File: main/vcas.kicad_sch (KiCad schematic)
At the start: 52 parts, among them U28 TL072CP, U29 TL072CP, U30 NSL-32SR3, U31 NSL-32SR3, U32 TL072CP, U33 TL072CP, U34 NSL-32SR3, U35 NSL-32SR3

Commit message: Switch to Thonk jacks.
Reduces use of extended parts.
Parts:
- C76, C77, C78, C79: LCSC Part # C277470 -> C45783
- R113, R116, R123, R126: LCSC Part # C136589 -> C4184
- U28, U29, U32, U33: LCSC Part # C67473 -> C6961
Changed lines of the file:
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@@
       (effects (font (size 1.27 1.27)) hide)
     )
-    (property "LCSC Part #" "C136589" (id 5) (at 149.86 120.015 0)
+    (property "LCSC Part #" "C4184" (id 5) (at 149.86 120.015 0)
       (effects (font (size 1.27 1.27)) hide)
     )
@@
       (effects (font (size 1.27 1.27)) hide)
     )
-    (property "LCSC Part #" "C67473" (id 6) (at 54.61 121.92 0)
+    (property "LCSC Part #" "C6961" (id 6) (at 54.61 121.92 0)
       (effects (font (size 1.27 1.27)) hide)
     )
@@
       (effects (font (size 1.27 1.27)) hide)
     )
-    (property "LCSC Part #" "C136589" (id 5) (at 148.59 52.07 0)
+    (property "LCSC Part #" "C4184" (id 5) (at 148.59 52.07 0)
       (effects (font (size 1.27 1.27)) hide)
     )
@@
       (effects (font (size 1.27 1.27)) hide)
     )
-    (property "LCSC Part #" "C277470" (id 5) (at 40.767 95.25 0)
+    (property "LCSC Part #" "C45783" (id 5) (at 40.767 95.25 0)
       (effects (font (size 1.27 1.27)) hide)
     )
@@
       (effects (font (size 1.27 1.27)) hide)
     )
-    (property "LCSC Part #" "C67473" (id 6) (at 82.55 105.41 0)
+    (property "LCSC Part #" "C6961" (id 6) (at 82.55 105.41 0)
       (effects (font (size 1.27 1.27)) hide)
     )
@@
       (effects (font (size 1.27 1.27)) hide)
     )
-    (property "LCSC Part #" "C277470" (id 5) (at 122.936 27.305 0)
+    (property "LCSC Part #" "C45783" (id 5) (at 122.936 27.305 0)
       (effects (font (size 1.27 1.27)) hide)
     )
@@
       (effects (font (size 1.27 1.27)) hide)
     )
-    (property "LCSC Part #" "C67473" (id 6) (at 135.255 54.61 0)
+    (property "LCSC Part #" "C6961" (id 6) (at 135.255 54.61 0)
       (effects (font (size 1.27 1.27)) hide)
     )
@@
       (effects (font (size 1.27 1.27)) hide)
     )
-    (property "LCSC Part #" "C277470" (id 5) (at 122.936 95.25 0)
+    (property "LCSC Part #" "C45783" (id 5) (at 122.936 95.25 0)
       (effects (font (size 1.27 1.27)) hide)
     )
@@
       (effects (font (size 1.27 1.27)) hide)
     )
-    (property "LCSC Part #" "C67473" (id 6) (at 213.995 35.56 0)
+    (property "LCSC Part #" "C6961" (id 6) (at 213.995 35.56 0)
       (effects (font (size 1.27 1.27)) hide)
     )
@@
       (effects (font (size 1.27 1.27)) hide)
     )
-    (property "LCSC Part #" "C67473" (id 6) (at 160.909 37.465 0)
+    (property "LCSC Part #" "C6961" (id 6) (at 160.909 37.465 0)
       (effects (font (size 1.27 1.27)) hide)
     )
@@
       (effects (font (size 1.27 1.27)) hide)
     )
-    (property "LCSC Part #" "C67473" (id 4) (at 203.2 35.56 0)
+    (property "LCSC Part #" "C6961" (id 4) (at 203.2 35.56 0)
       (effects (font (size 1.27 1.27)) hide)
     )
@@
       (effects (font (size 1.27 1.27)) hide)
     )
-    (property "LCSC Part #" "C67473" (id 6) (at 79.375 37.465 0)
+    (property "LCSC Part #" "C6961" (id 6) (at 79.375 37.465 0)
       (effects (font (size 1.27 1.27)) hide)
     )
@@
       (effects (font (size 1.27 1.27)) hide)
     )
-    (property "LCSC Part #" "C67473" (id 6) (at 161.544 105.41 0)
+    (property "LCSC Part #" "C6961" (id 6) (at 161.544 105.41 0)
       (effects (font (size 1.27 1.27)) hide)
     )
@@
       (effects (font (size 1.27 1.27)) hide)
     )
-    (property "LCSC Part #" "C67473" (id 6) (at 226.06 35.56 0)
+    (property "LCSC Part #" "C6961" (id 6) (at 226.06 35.56 0)
       (effects (font (size 1.27 1.27)) hide)
     )
@@
       (effects (font (size 1.27 1.27)) hide)
     )
-    (property "LCSC Part #" "C277470" (id 5) (at 40.767 27.305 0)
+    (property "LCSC Part #" "C45783" (id 5) (at 40.767 27.305 0)
       (effects (font (size 1.27 1.27)) hide)
     )
@@
       (effects (font (size 1.27 1.27)) hide)
     )
-    (property "LCSC Part #" "C67473" (id 4) (at 214.63 35.56 0)
+    (property "LCSC Part #" "C6961" (id 4) (at 214.63 35.56 0)
       (effects (font (size 1.27 1.27)) hide)
     )
@@
       (effects (font (size 1.27 1.27)) hide)
     )
-    (property "LCSC Part #" "C67473" (id 6) (at 53.975 55.245 0)
+    (property "LCSC Part #" "C6961" (id 6) (at 53.975 55.245 0)
       (effects (font (size 1.27 1.27)) hide)
     )
@@
       (effects (font (size 1.27 1.27)) hide)
     )
-    (property "LCSC Part #" "C67473" (id 6) (at 135.89 122.555 0)
+    (property "LCSC Part #" "C6961" (id 6) (at 135.89 122.555 0)
       (effects (font (size 1.27 1.27)) hide)
     )
@@
       (effects (font (size 1.27 1.27)) hide)
     )
-    (property "LCSC Part #" "C136589" (id 5) (at 68.58 119.38 0)
+    (property "LCSC Part #" "C4184" (id 5) (at 68.58 119.38 0)
       (effects (font (size 1.27 1.27)) hide)
     )
@@
       (effects (font (size 1.27 1.27)) hide)
     )
-    (property "LCSC Part #" "C136589" (id 5) (at 67.31 52.705 0)
-      (effects (font (size 1.27 1.27)) hide)
-    )
+    (property "LCSC Part #" "C4184" (id 5) (at 67.31 52.705 0)
+      (effects (font (size 1.27 1.27)) hide)
+    )

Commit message: Version 1.0
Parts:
- removed C76, C77, C78, C79: 22uF, Capacitor_SMD:C_0805_2012Metric_Pad1.18x1.45mm_HandSolder, symbol Device:C_Small
- R118, R119, R128, R129: value 430 -> 1.21K; LCSC Part # C23170 -> C22835
- RV12, RV13, RV16, RV17: value 500 -> 1K; LCSC Part # C116324 -> C50204
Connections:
- net SIG1*: now reaches U31.4
- net SIG3*: now reaches U30.4
- net SIG4*: now reaches U34.4
- net SIG2*: now reaches U35.4
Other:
- note added: "Bump 3.5V sig to 10Vpp Gain = 2.86"
- note added: "Input: 3.5Vpp"
- note removed: "Bump 9V sig to 10V Gain = 1.111"

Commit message: v1.0
Docs still need work.
Oscillators.sch not used. Saved just in case.
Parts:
- RV10, RV11, RV14, RV15: Digi-Key Part PTV09A-4225F-B102-ND -> PTV09A-4020F-B102-ND
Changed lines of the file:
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@@
       (effects (font (size 1.27 1.27)) hide)
     )
-    (property "Digi-Key Part" "PTV09A-4225F-B102-ND" (id 4) (at 163.83 62.23 0)
+    (property "Digi-Key Part" "PTV09A-4020F-B102-ND" (id 4) (at 163.83 62.23 0)
       (effects (font (size 1.27 1.27)) hide)
     )
@@
       (effects (font (size 1.27 1.27)) hide)
     )
-    (property "Digi-Key Part" "PTV09A-4225F-B102-ND" (id 4) (at 82.55 62.23 0)
+    (property "Digi-Key Part" "PTV09A-4020F-B102-ND" (id 4) (at 82.55 62.23 0)
       (effects (font (size 1.27 1.27)) hide)
     )
@@
       (effects (font (size 1.27 1.27)) hide)
     )
-    (property "Digi-Key Part" "PTV09A-4225F-B102-ND" (id 4) (at 160.655 133.35 0)
+    (property "Digi-Key Part" "PTV09A-4020F-B102-ND" (id 4) (at 160.655 133.35 0)
       (effects (font (size 1.27 1.27)) hide)
     )
@@
       (effects (font (size 1.27 1.27)) hide)
     )
-    (property "Digi-Key Part" "PTV09A-4225F-B102-ND" (id 4) (at 80.01 133.35 0)
-      (effects (font (size 1.27 1.27)) hide)
-    )
+    (property "Digi-Key Part" "PTV09A-4020F-B102-ND" (id 4) (at 80.01 133.35 0)
+      (effects (font (size 1.27 1.27)) hide)
+    )

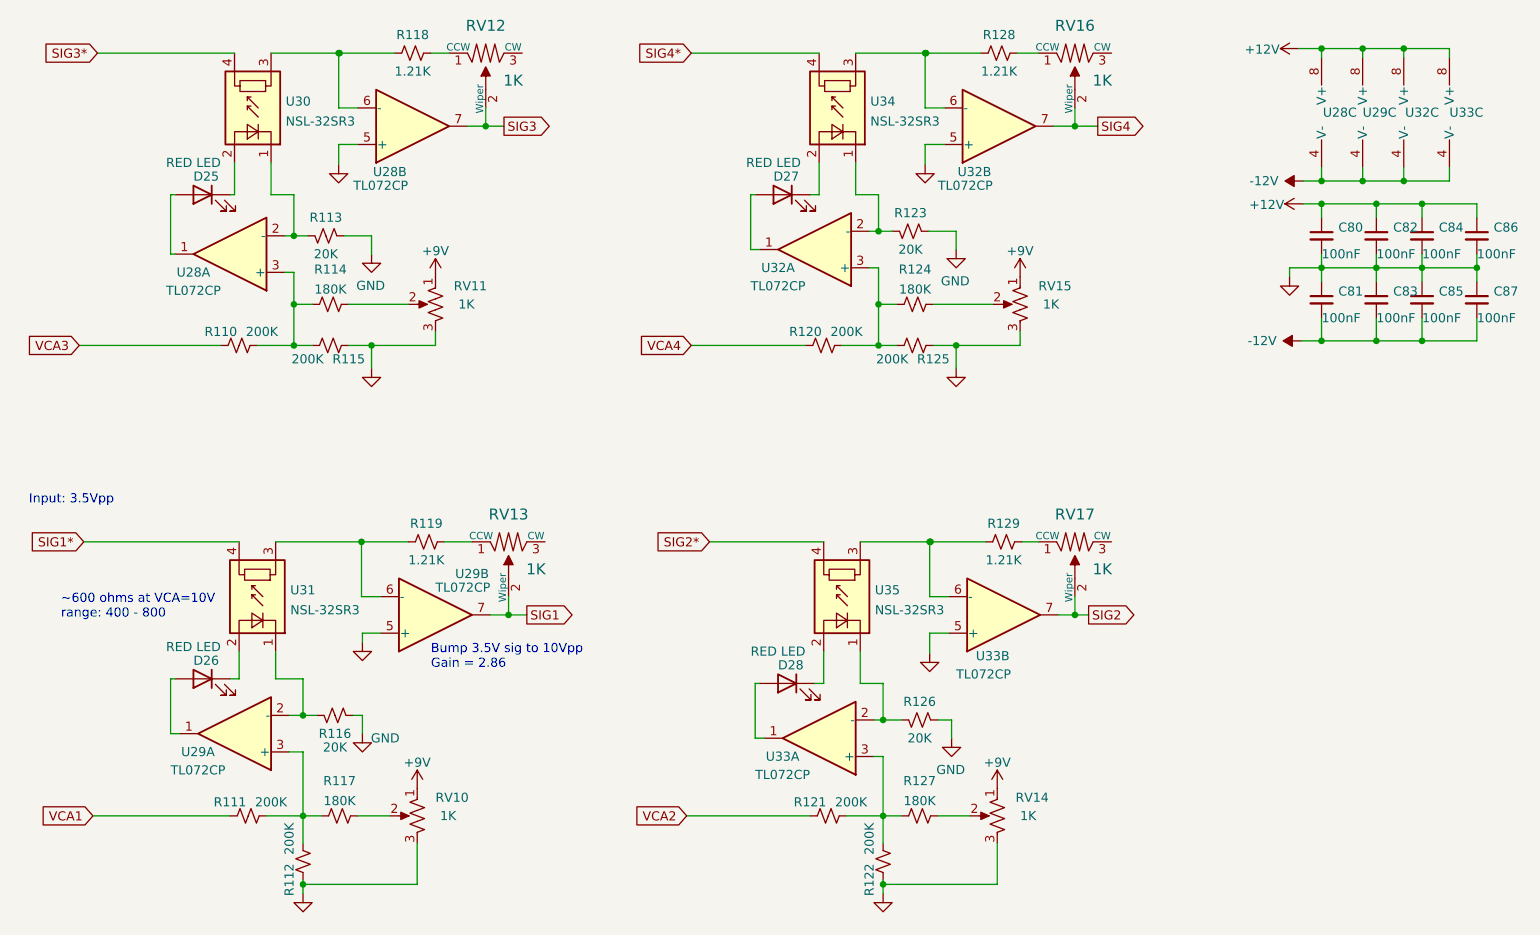
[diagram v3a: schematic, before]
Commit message: Work in progress
Adds User Manual
Changes CV range to 0 - 8V
Adds spice vactrol test circuit.
Adds VCA spice study
Updates other spice and excel files.
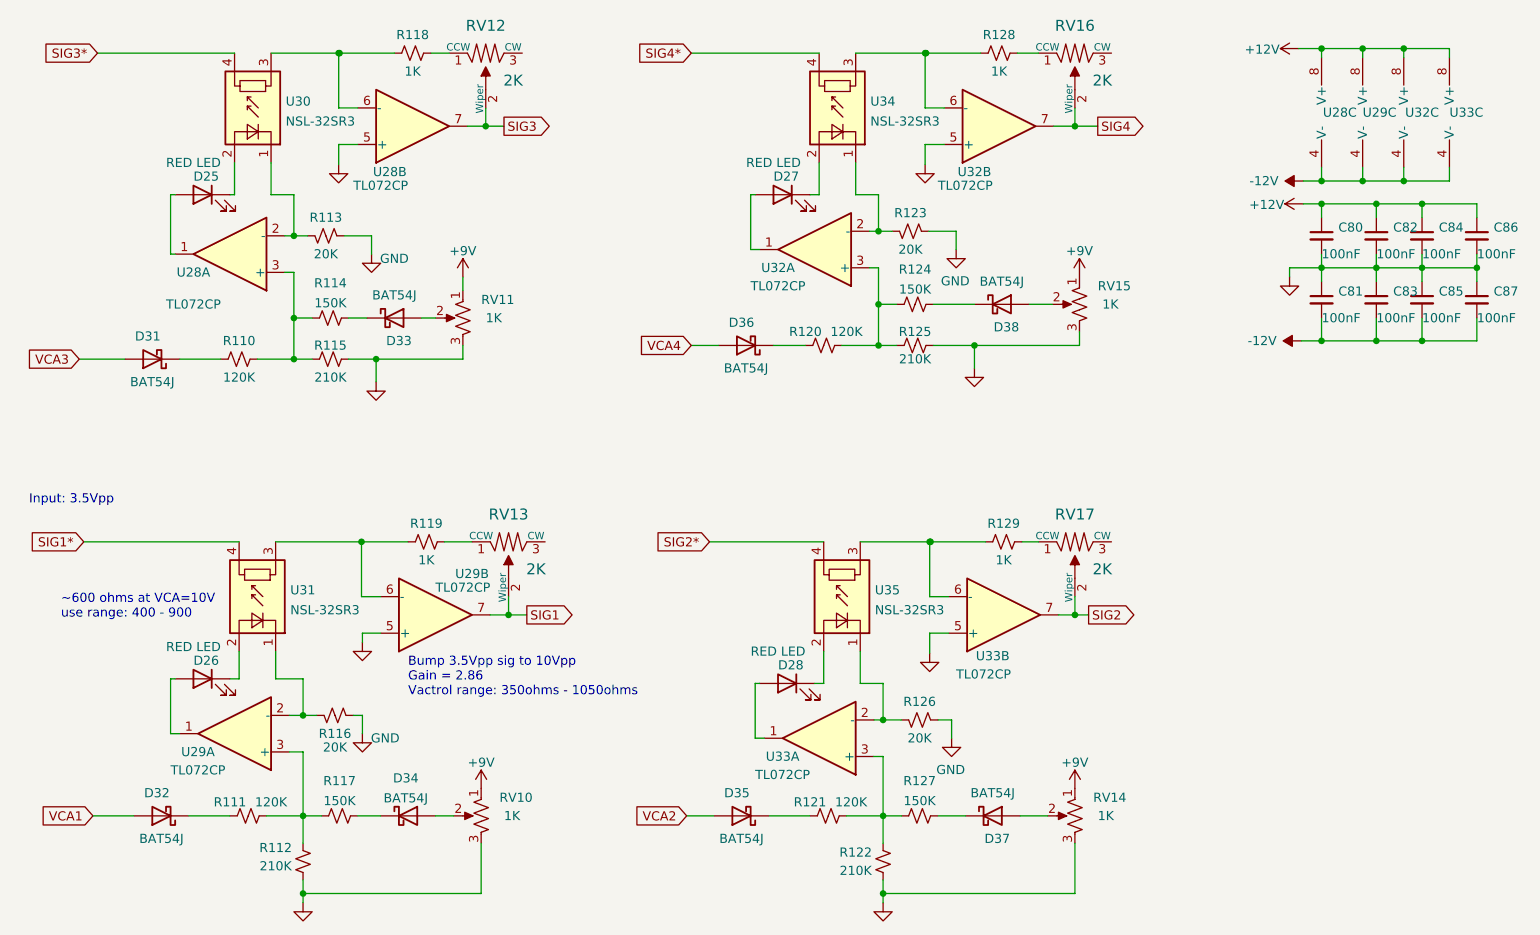
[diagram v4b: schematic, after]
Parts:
- added D31, D32, D33, D34, D35, D36, D37, D38: BAT54J, Diode_SMD:D_SOD-323F, symbol Diode:BAT54J
- R110, R111, R120, R121: value 200K -> 120K; LCSC Part # C25811 -> C25808
- R112, R115, R122, R125: value 200K -> 210K; LCSC Part # C25811 -> C227705
- R114, R117, R124, R127: value 180K -> 150K; LCSC Part # C3016400 -> C22807
- R118, R119, R128, R129: value 1.21K -> 1K; LCSC Part # C22835 -> C21190
- RV12, RV13, RV16, RV17: value 1K -> 2K; LCSC Part # C50204 -> C116322
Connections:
- net VCA1: now also D32.2 (A); no longer R111.1
- net VCA2: now also D35.2 (A); no longer R121.1
- net VCA3: now also D31.2 (A); no longer R110.1
- net VCA4: now also D36.2 (A); no longer R120.1
- net at RV15.2: now also D38.2 (A); no longer R124.2
- net at R114.2: now also D33.1 (K); no longer RV11.2
- net at R127.2: now also D37.1 (K); no longer RV14.2
- net at RV10.2: now also D34.2 (A); no longer R117.2
- new net: D36.1 (K), R120.1
- new net: D32.1 (K), R111.1
- new net: D35.1 (K), R121.1
- new net: D31.1 (K), R110.1
- new net: D37.2 (A), RV14.2
- new net: D33.2 (A), RV11.2
- new net: D38.1 (K), R124.2
- new net: D34.1 (K), R117.2
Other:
- note added: "Bump 3.5Vpp sig to 10Vpp Gain = 2.86 Vactrol range: 350ohms - 1050ohms"
- note added: "~600 ohms at VCA=10V use range: 400 - 900"
- note removed: "Bump 3.5V sig to 10Vpp Gain = 2.86"
- note removed: "~600 ohms at VCA=10V range: 400 - 800"
- title: (none) -> Twangilizer
- moved on the sheet: R110, R114, R115, RV10, RV11, RV14, RV15

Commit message: Latest gain plan.
Version 1.1
Sent to JLCPCB
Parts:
- RV12, RV13, RV16, RV17: value 2K -> 5K; LCSC Part # C116322 -> C81349
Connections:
- net SIG1* renamed VCF1
- net SIG2* renamed VCF2
- net SIG3* renamed VCF3
- net SIG4* renamed VCF4
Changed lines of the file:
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@@
     (effects (font (size 1.27 1.27)) (justify left bottom))
   )
-  (global_label "SIG1*" (shape input) (at 33.655 95.25 180) (fields_autoplaced)
+  (global_label "VCF1" (shape input) (at 33.655 95.25 180) (fields_autoplaced)
     (effects (font (size 1.27 1.27)) (justify right))
-    (property "Intersheet References" "${INTERSHEET_REFS}" (id 0) (at 25.9805 95.1706 0)
+    (property "Intersheet References" "${INTERSHEET_REFS}" (id 0) (at 26.5852 95.1706 0)
       (effects (font (size 1.27 1.27)) (justify right) hide)
     )
@@
     )
   )
-  (global_label "SIG2*" (shape input) (at 120.65 95.25 180) (fields_autoplaced)
+  (global_label "VCF2" (shape input) (at 120.65 95.25 180) (fields_autoplaced)
     (effects (font (size 1.27 1.27)) (justify right))
-    (property "Intersheet References" "${INTERSHEET_REFS}" (id 0) (at 112.9755 95.1706 0)
+    (property "Intersheet References" "${INTERSHEET_REFS}" (id 0) (at 113.5802 95.1706 0)
       (effects (font (size 1.27 1.27)) (justify right) hide)
     )
@@
     )
   )
-  (global_label "SIG4*" (shape input) (at 118.11 27.305 180) (fields_autoplaced)
+  (global_label "VCF4" (shape input) (at 118.11 27.305 180) (fields_autoplaced)
     (effects (font (size 1.27 1.27)) (justify right))
-    (property "Intersheet References" "${INTERSHEET_REFS}" (id 0) (at 110.4355 27.2256 0)
+    (property "Intersheet References" "${INTERSHEET_REFS}" (id 0) (at 111.0402 27.2256 0)
       (effects (font (size 1.27 1.27)) (justify right) hide)
     )
   )
-  (global_label "SIG3*" (shape input) (at 35.56 27.305 180) (fields_autoplaced)
+  (global_label "VCF3" (shape input) (at 35.56 27.305 180) (fields_autoplaced)
     (effects (font (size 1.27 1.27)) (justify right))
-    (property "Intersheet References" "${INTERSHEET_REFS}" (id 0) (at 27.8855 27.2256 0)
+    (property "Intersheet References" "${INTERSHEET_REFS}" (id 0) (at 28.4902 27.2256 0)
       (effects (font (size 1.27 1.27)) (justify right) hide)
     )
@@
       (effects (font (size 1.524 1.524)))
     )
-    (property "Value" "2K" (id 1) (at 175.26 99.06 0)
+    (property "Value" "5K" (id 1) (at 175.26 99.06 0)
       (effects (font (size 1.524 1.524)))
     )
@@
       (effects (font (size 1.27 1.27)) hide)
     )
-    (property "LCSC Part #" "C116322" (id 6) (at 171.45 95.25 0)
+    (property "LCSC Part #" "C81349" (id 6) (at 171.45 95.25 0)
       (effects (font (size 1.27 1.27)) hide)
     )
@@
       (effects (font (size 1.524 1.524)))
     )
-    (property "Value" "2K" (id 1) (at 96.52 99.06 0)
+    (property "Value" "5K" (id 1) (at 96.52 99.06 0)
       (effects (font (size 1.524 1.524)))
     )
@@
       (effects (font (size 1.27 1.27)) hide)
     )
-    (property "LCSC Part #" "C116322" (id 6) (at 92.71 95.25 0)
+    (property "LCSC Part #" "C81349" (id 6) (at 92.71 95.25 0)
       (effects (font (size 1.27 1.27)) hide)
     )
@@
       (effects (font (size 1.524 1.524)))
     )
-    (property "Value" "2K" (id 1) (at 93.345 31.115 0)
+    (property "Value" "5K" (id 1) (at 93.345 31.115 0)
       (effects (font (size 1.524 1.524)))
     )
@@
       (effects (font (size 1.27 1.27)) hide)
     )
-    (property "LCSC Part #" "C116322" (id 6) (at 89.535 27.305 0)
+    (property "LCSC Part #" "C81349" (id 6) (at 89.535 27.305 0)
       (effects (font (size 1.27 1.27)) hide)
     )
@@
       (effects (font (size 1.524 1.524)))
     )
-    (property "Value" "2K" (id 1) (at 175.26 31.115 0)
+    (property "Value" "5K" (id 1) (at 175.26 31.115 0)
       (effects (font (size 1.524 1.524)))
     )
@@
       (effects (font (size 1.27 1.27)) hide)
     )
-    (property "LCSC Part #" "C116322" (id 6) (at 171.45 27.305 0)
-      (effects (font (size 1.27 1.27)) hide)
-    )
+    (property "LCSC Part #" "C81349" (id 6) (at 171.45 27.305 0)
+      (effects (font (size 1.27 1.27)) hide)
+    )

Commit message: v2.0
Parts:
- D25, D26, D27, D28: value RED LED -> YELLOW LED; Digi-Key Part 732-5005-ND -> 732-5010-ND
- RV12, RV13, RV16, RV17: footprint Potentiometer_SMD:Potentiometer_Bourns_3224W_Vertical -> greenface:Trimpot_3.8mmx3.6mm_TC33X-2-103E; symbol dk_Trimmer-Potentiometers:TC33X-2-103E -> greenface:TC33X-2-103E; Category (none) -> Potentiometers, Variable Resistors; DK_Datasheet_Link (none) -> https://www.bourns.com/docs/Product-Datasheets/TC33.pdf; DK_Detail_Page (none) -> /product-detail/en/bourns-inc/TC33X-2-103E/TC33X-103ETR-ND/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; Description_1 (none) -> TRIMMER 10K OHM 0.1W J LEAD TOP; Digi-Key_PN (none) -> TC33X-103ETR-ND; Family (none) -> Trimmer Potentiometers; MPN (none) -> TC33X-2-103E; Manufacturer (none) -> Bourns Inc.; Status (none) -> Active
- U30, U31, U34, U35: footprint sputterizer:NSL-32SR3 -> greenface:NSL-32SR3
